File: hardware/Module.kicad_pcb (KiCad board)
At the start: 2 copper layers, 93.1 x 98.9 mm, 96 parts, among them J1 Power, J10 Jack, J11 A I/O, J12 Debug, J13 A IFACE, J2 B IFACE, J3 B I/O, J4 Jack, J5 Jack, J6 Jack, J7 Jack, J8 Jack, J9 Jack, SW2 Button, U1 MCP6004, U4 LM4040C10, U6 TL072, U9 MCP6002

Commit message: Prepare the schematic
Signed-off-by: Petr Horacek <hrck@protonmail.com>
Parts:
- moved A1 73.6 mm to (234.5, 48.2)
- moved RV4 53.4 mm to (229.4, 77.3)
- moved J5 49.9 mm to (237.4, 100.8)
- moved RV3 15.3 mm to (209.1, 95.6)

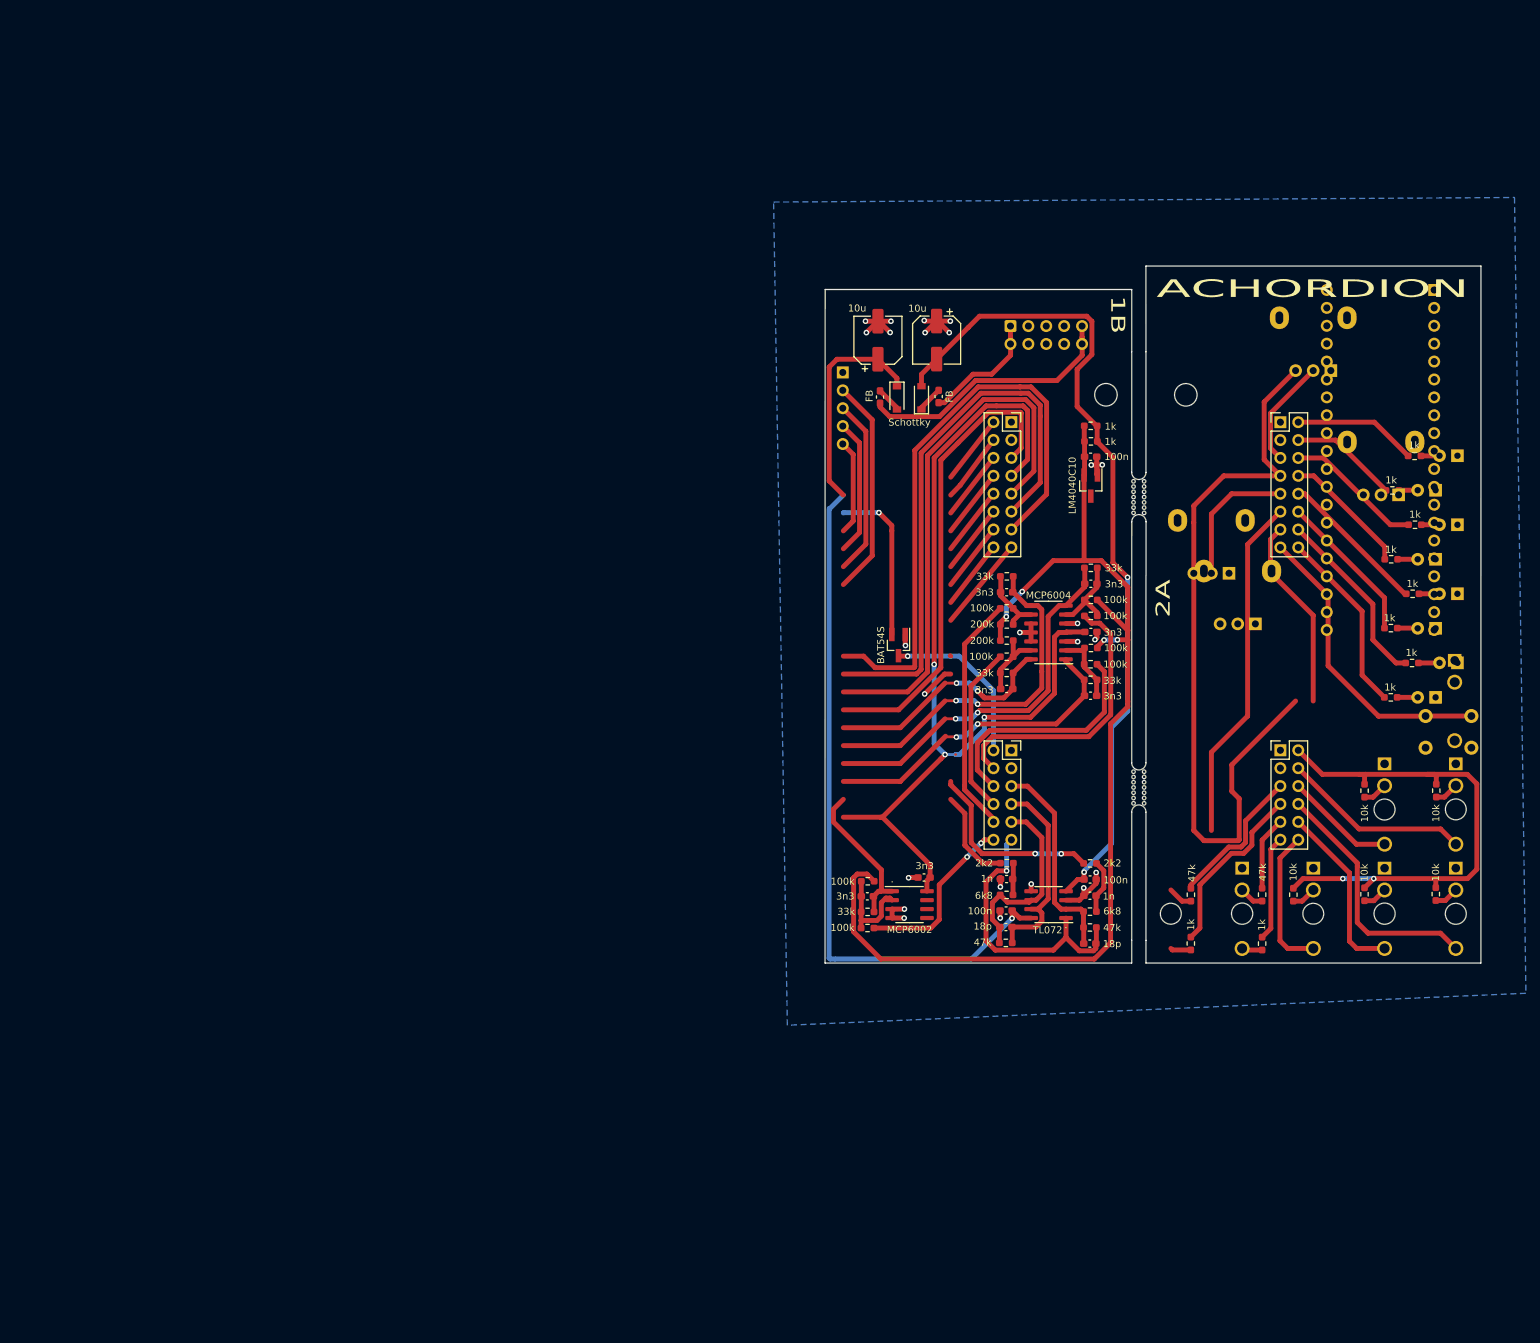
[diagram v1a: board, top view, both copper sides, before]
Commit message: Add SD card footprint
Signed-off-by: Petr Horacek <hrck@protonmail.com>
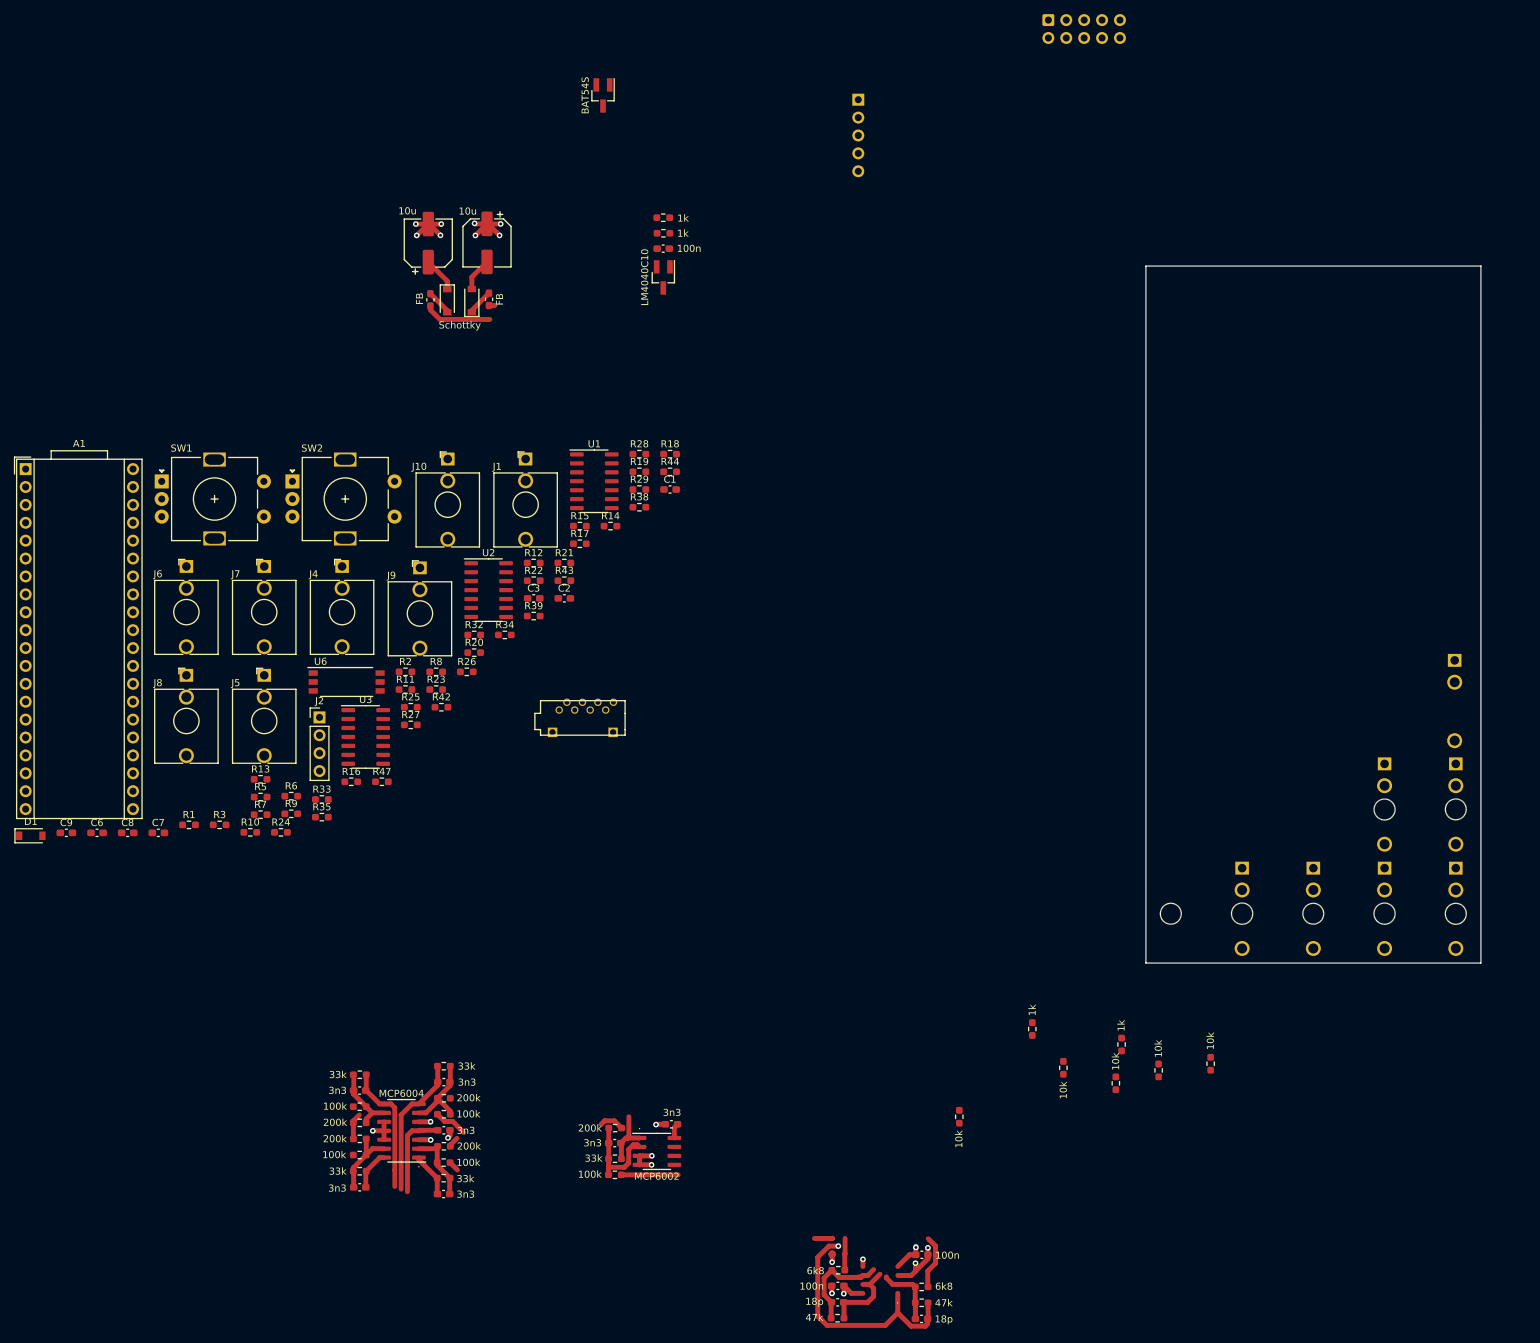
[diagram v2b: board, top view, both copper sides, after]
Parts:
- removed C35, C37: 1n, Capacitor_SMD:C_0603_1608Metric_Pad1.08x0.95mm_HandSolder
- removed D10, D5, D6, D7, D8, D9: LED, LED_THT:LED_D3.0mm
- removed the D3 at (234.7, 106.0)
- removed the D4 at (237.8, 101.2)
- removed the J11 at (212.6, 113.6)
- removed the J3 at (174.4, 113.6)
- removed the R36 at (231.3, 101.2)
- removed the R37 at (228.3, 96.2)
- removed the R40 at (231.7, 81.5)
- removed the R41 at (228.5, 76.7)
- removed the R50 at (199.9, 134.1)
- removed the R51 at (210.0, 134.1)
- removed REF** (x2): MountingHole_3.2mm_M3, MountingHole:MountingHole_3.2mm_M3
- removed RV1, RV2, RV3, RV4: B10k, Potentiometer_THT:Potentiometer_Alpha_RD901F-40-00D_Single_Vertical
- removed mouse-bite-2mm-slot (x2): VAL**, Panelization:mouse-bite-2mm-slot
- added C1: 100n, Capacitor_SMD:C_0603_1608Metric_Pad1.08x0.95mm_HandSolder, F.Cu at (126.0, 76.5)
- added C2: 18p, Capacitor_SMD:C_0603_1608Metric_Pad1.08x0.95mm_HandSolder, F.Cu at (111.0, 92.0)
- added C3: 18p, Capacitor_SMD:C_0603_1608Metric_Pad1.08x0.95mm_HandSolder, F.Cu at (106.7, 92.0)
- added C6: 100n, Capacitor_SMD:C_0603_1608Metric_Pad1.08x0.95mm_HandSolder, F.Cu at (44.7, 125.3)
- added C7: 100n, Capacitor_SMD:C_0603_1608Metric_Pad1.08x0.95mm_HandSolder, F.Cu at (53.4, 125.3)
- added C8: 100n, Capacitor_SMD:C_0603_1608Metric_Pad1.08x0.95mm_HandSolder, F.Cu at (49.0, 125.3)
- added C9: 100n, Capacitor_SMD:C_0603_1608Metric_Pad1.08x0.95mm_HandSolder, F.Cu at (40.3, 125.3)
- added D1: Schottky, Diode_SMD:D_SOD-123, F.Cu at (35.3, 125.7)
- added J1: Jack, Connector_Audio:Jack_3.5mm_QingPu_WQP-PJ398SM_Vertical_CircularHoles, F.Cu at (105.5, 72.2)
- added J10: Jack, Connector_Audio:Jack_3.5mm_QingPu_WQP-PJ398SM_Vertical_CircularHoles, F.Cu at (94.5, 72.2)
- added J4: Jack, Connector_Audio:Jack_3.5mm_QingPu_WQP-PJ398SM_Vertical_CircularHoles, F.Cu at (79.5, 87.5)
- added J5: Jack, Connector_Audio:Jack_3.5mm_QingPu_WQP-PJ398SM_Vertical_CircularHoles, F.Cu at (68.4, 102.9)
- added J6: Jack, Connector_Audio:Jack_3.5mm_QingPu_WQP-PJ398SM_Vertical_CircularHoles, F.Cu at (57.4, 87.5)
- added J7: Jack, Connector_Audio:Jack_3.5mm_QingPu_WQP-PJ398SM_Vertical_CircularHoles, F.Cu at (68.4, 87.5)
- added J8: Jack, Connector_Audio:Jack_3.5mm_QingPu_WQP-PJ398SM_Vertical_CircularHoles, F.Cu at (57.4, 102.9)
- added J9: Jack, Connector_Audio:Jack_3.5mm_QingPu_WQP-PJ398SM_Vertical_CircularHoles, F.Cu at (90.5, 87.7)
- added R1: 33R, Resistor_SMD:R_0603_1608Metric_Pad0.98x0.95mm_HandSolder, F.Cu at (57.7, 124.2)
- added R10: 100k, Resistor_SMD:R_0603_1608Metric_Pad0.98x0.95mm_HandSolder, F.Cu at (66.4, 125.2)
- added R12: 6k8, Resistor_SMD:R_0603_1608Metric_Pad0.98x0.95mm_HandSolder, F.Cu at (106.7, 87.0)
- added R13: 6k8, Resistor_SMD:R_0603_1608Metric_Pad0.98x0.95mm_HandSolder, F.Cu at (67.9, 117.7)
- added R14: 100k, Resistor_SMD:R_0603_1608Metric_Pad0.98x0.95mm_HandSolder, F.Cu at (117.6, 81.7)
- added R15: 100k, Resistor_SMD:R_0603_1608Metric_Pad0.98x0.95mm_HandSolder, F.Cu at (113.2, 81.7)
- added R16: 200k, Resistor_SMD:R_0603_1608Metric_Pad0.98x0.95mm_HandSolder, F.Cu at (80.8, 118.0)
- added R17: 200k, Resistor_SMD:R_0603_1608Metric_Pad0.98x0.95mm_HandSolder, F.Cu at (113.2, 84.2)
- added R18: 1k, Resistor_SMD:R_0603_1608Metric_Pad0.98x0.95mm_HandSolder, F.Cu at (126.0, 71.5)
- added R19: 1k, Resistor_SMD:R_0603_1608Metric_Pad0.98x0.95mm_HandSolder, F.Cu at (121.7, 74.0)
- added R2: 220R, Resistor_SMD:R_0603_1608Metric_Pad0.98x0.95mm_HandSolder, F.Cu at (88.5, 102.4)
- added R20: 100k, Resistor_SMD:R_0603_1608Metric_Pad0.98x0.95mm_HandSolder, F.Cu at (98.2, 99.7)
- added R21: 100k, Resistor_SMD:R_0603_1608Metric_Pad0.98x0.95mm_HandSolder, F.Cu at (111.0, 87.0)
- added R22: 33k, Resistor_SMD:R_0603_1608Metric_Pad0.98x0.95mm_HandSolder, F.Cu at (106.7, 89.5)
- added R23: 33k, Resistor_SMD:R_0603_1608Metric_Pad0.98x0.95mm_HandSolder, F.Cu at (92.8, 104.9)
- added R24: 33k, Resistor_SMD:R_0603_1608Metric_Pad0.98x0.95mm_HandSolder, F.Cu at (70.8, 125.2)
- added R25: 33k, Resistor_SMD:R_0603_1608Metric_Pad0.98x0.95mm_HandSolder, F.Cu at (89.2, 107.5)
- added R26: 100k, Resistor_SMD:R_0603_1608Metric_Pad0.98x0.95mm_HandSolder, F.Cu at (97.2, 102.4)
- added R27: 100k, Resistor_SMD:R_0603_1608Metric_Pad0.98x0.95mm_HandSolder, F.Cu at (89.2, 110.0)
- added R28: 100k, Resistor_SMD:R_0603_1608Metric_Pad0.98x0.95mm_HandSolder, F.Cu at (121.7, 71.5)
- added R29: 100k, Resistor_SMD:R_0603_1608Metric_Pad0.98x0.95mm_HandSolder, F.Cu at (121.7, 76.5)
- added R3: 10R, Resistor_SMD:R_0603_1608Metric_Pad0.98x0.95mm_HandSolder, F.Cu at (62.1, 124.2)
- added R32: 100R, Resistor_SMD:R_0603_1608Metric_Pad0.98x0.95mm_HandSolder, F.Cu at (98.2, 97.2)
- added R33: 100R, Resistor_SMD:R_0603_1608Metric_Pad0.98x0.95mm_HandSolder, F.Cu at (76.6, 120.5)
- added R34: 1k, Resistor_SMD:R_0603_1608Metric_Pad0.98x0.95mm_HandSolder, F.Cu at (102.6, 97.2)
- added R43: 47k, Resistor_SMD:R_0603_1608Metric_Pad0.98x0.95mm_HandSolder, F.Cu at (111.0, 89.5)
- added R44: 47k, Resistor_SMD:R_0603_1608Metric_Pad0.98x0.95mm_HandSolder, F.Cu at (126.0, 74.0)
- added R47: 10k, Resistor_SMD:R_0603_1608Metric_Pad0.98x0.95mm_HandSolder, F.Cu at (85.1, 118.0)
- added R5: 10k, Resistor_SMD:R_0603_1608Metric_Pad0.98x0.95mm_HandSolder, F.Cu at (67.9, 120.2)
- added R6: 47k, Resistor_SMD:R_0603_1608Metric_Pad0.98x0.95mm_HandSolder, F.Cu at (72.2, 120.1)
- added R8: 33k, Resistor_SMD:R_0603_1608Metric_Pad0.98x0.95mm_HandSolder, F.Cu at (92.8, 102.4)
- added R9: 33k, Resistor_SMD:R_0603_1608Metric_Pad0.98x0.95mm_HandSolder, F.Cu at (72.2, 122.6)
- added SW1: Encoder, Rotary_Encoder:RotaryEncoder_Alps_EC11E-Switch_Vertical_H20mm, F.Cu at (53.9, 75.4)
- added U2: TL074, Package_SO:SOIC-14_3.9x8.7mm_P1.27mm, F.Cu at (100.3, 90.8)
- added U3: TL074, Package_SO:SOIC-14_3.9x8.7mm_P1.27mm, F.Cu at (82.8, 111.7)
- added U4: MCP6004, Package_SO:SOIC-14_3.9x8.7mm_P1.27mm, F.Cu at (87.9, 167.6)
- A1: moved to F.Cu
- J13: value A IFACE -> Micro_SD; footprint Connector_PinHeader_2.54mm:PinHeader_2x08_P2.54mm_Vertical -> Custom:microsd_connector
- J2: value B IFACE -> OLED; footprint Connector_PinSocket_2.54mm:PinSocket_2x08_P2.54mm_Vertical -> Connector_PinHeader_2.54mm:PinHeader_1x04_P2.54mm_Vertical
- R11: value 2k2 -> 100k
- R38, R39, R42: value 1k -> 47k
- R48: renamed from R20; value 100k -> 200k
- R52: renamed from R23; value 100k -> 200k
- R59: renamed from R17; value 100k -> 200k
- R7: value 2k2 -> 47k
- SW2: value Button -> Encoder; footprint Button_Switch_THT:SW_PUSH_6mm -> Rotary_Encoder:RotaryEncoder_Alps_EC11E-Switch_Vertical_H20mm; moved to F.Cu
- U1: value MCP6004 -> TL074
- U6: value TL072 -> TLP2361; footprint Package_SO:SOIC-8_3.9x4.9mm_P1.27mm -> Package_SO:SO-6L_10x3.84mm_P1.27mm
- moved A1 201.5 mm to (34.5, 73.7), turned to 0 degrees
- moved SW2 170.6 mm to (72.4, 75.4), turned to 0 degrees
- moved R35 152.7 mm to (76.6, 123.0)
- moved R42 142.7 mm to (93.6, 107.5)
- moved R39 122.0 mm to (106.7, 94.5)
- moved R7 117.9 mm to (67.9, 122.7)
- moved R65 115.9 mm to (82.0, 159.6)
- moved C17 115.9 mm to (93.9, 176.6)
- moved C18 115.9 mm to (82.0, 161.9)
- moved R50 115.9 mm to (82.0, 168.7)
- moved R59 115.9 mm to (93.9, 169.8)
- moved R61 115.9 mm to (82.0, 166.4)
- moved C13 115.9 mm to (82.0, 175.6)
- moved C15 115.9 mm to (93.9, 167.5)
- moved R49 115.9 mm to (93.9, 165.2)
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- renumbered C33 to C10, C34 to C11, C41 to C12, C43 to C13, C44 to C14, C46 to C15, C48 to C16, C40 to C17, C42 to C18, C38 to C4, C36 to C5, D11 to D2, D1 to D3, D2 to D4, J5 to J11, J4 to J12, J6 to J14, J8 to J15, J10 to J16, J1 to J17, J7 to J18, J9 to J19, J12 to J3, R12 to R30, R8 to R31, R13 to R36, R9 to R37, R48 to R4, R14 to R40, R10 to R41, R43 to R45, R21 to R49, R27 to R50, R28 to R51, R30 to R53, R22 to R54, R29 to R55, R31 to R56, R45 to R57, R47 to R58, R18 to R60, R24 to R61, R25 to R62, R4 to R63, R19 to R64, R26 to R65, R5 to R66, U9 to U5, U4 to U7
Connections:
- A1 pad 1: B_LED8 -> Net-(A1-Pad1)
- A1 pad 11: B_PROBE -> Net-(A1-Pad11)
- A1 pad 12: VERSION_A -> OLED_SCL
- A1 pad 13: VERSION_A -> OLED_SDA
- A1 pad 14: VERSION_A -> Net-(A1-Pad14)
- A1 pad 15: VERSION_A -> Net-(A1-Pad15)
- A1 pad 16: Net-(A1-Pad16) -> AUDIO_IN1
- A1 pad 17: Net-(A1-Pad17) -> AUDIO_IN2
- A1 pad 18: DAC1 -> AUDIO_OUT1
- A1 pad 19: DAC2 -> AUDIO_OUT2
- A1 pad 2: B_LED7 -> SD_D3
- A1 pad 20: VERSION_A -> GND
- A1 pad 27: B_POT1 -> MIDI_OUT
- A1 pad 28: B_POT2 -> MIDI_IN
- A1 pad 29: B_POT4 -> DAC1
- A1 pad 3: B_LED6 -> SD_D2
- A1 pad 30: B_POT3 -> DAC2
- A1 pad 31: Net-(A1-Pad31) -> ENC1_A
- A1 pad 32: Net-(A1-Pad32) -> ENC1_B
- A1 pad 33: Net-(A1-Pad33) -> ENC2_A
- A1 pad 34: GPIO1 -> ENC2_B
- A1 pad 35: GPIO2 -> Net-(A1-Pad35)
- A1 pad 36: GPIO3 -> Net-(A1-Pad36)
- A1 pad 37: GPIO4 -> Net-(A1-Pad37)
- A1 pad 4: B_LED5 -> SD_D1
- A1 pad 40: VERSION_A -> GND
- A1 pad 5: B_LED4 -> SD_D0
- A1 pad 6: B_LED3 -> SD_CMD
- A1 pad 7: B_LED2 -> SD_CK
- A1 pad 8: B_LED1 -> ENC1_CLICK
- A1 pad 9: B_BUTTON -> ENC2_CLICK
- C10 pad 2: VERSION_A -> GND
- C11 pad 1: VERSION_A -> GND
- C12 pad 2: Net-(C41-Pad2) -> Net-(C12-Pad2)
- C13 pad 2: Net-(C43-Pad2) -> Net-(C13-Pad2)
- C15 pad 1: VERSION_A -> GND
- C16 pad 1: VERSION_A -> GND
- C17 pad 2: Net-(C40-Pad2) -> Net-(C17-Pad2)
- C18 pad 2: Net-(C42-Pad2) -> Net-(C18-Pad2)
- C19 pad 2: VERSION_A -> GND
- C20 pad 1: VERSION_A -> GND
- C21 pad 2: VERSION_A -> GND
- C4 pad 1: B_OUT2_MAIN -> Net-(C4-Pad1)
- C4 pad 2: B_OUT1_FALL -> Net-(C4-Pad2)
- C5 pad 1: B_OUT1_MAIN -> Net-(C5-Pad1)
- C5 pad 2: B_OUT2_FALL -> Net-(C5-Pad2)
- D2 pad 1: VERSION_A -> GND
- D2 pad 3: B_PROBE -> PROBE
- J11 pad S: VERSION_A -> GND
- J12 pad S: VERSION_A -> GND
- J14 pad S: VERSION_A -> GND
- J14 pad T: A_CV1_IN -> Net-(J14-PadT)
- J15 pad S: VERSION_A -> GND
- J15 pad T: A_CV3_IN -> Net-(J15-PadT)
- J16 pad S: VERSION_A -> GND
- J16 pad T: A_CV5_IN -> Net-(J16-PadT)
- J16 pad TN: Net-(J10-PadTN) -> Net-(J16-PadTN)
- J17 pad 3: VERSION_A -> GND
- J17 pad 4: VERSION_A -> GND
- J17 pad 5: VERSION_A -> GND
- J17 pad 6: VERSION_A -> GND
- J17 pad 7: VERSION_A -> GND
- J17 pad 8: VERSION_A -> GND
- J18 pad S: VERSION_A -> GND
- J18 pad T: A_CV2_IN -> Net-(J18-PadT)
- J19 pad S: VERSION_A -> GND
- J19 pad T: A_CV4_IN -> Net-(J19-PadT)
- J2 pad 1: VERSION_A -> +3V3
- J2 pad 2: B_LED8 -> GND
- J2 pad 3: VERSION_A -> OLED_SCL
- J2 pad 4: B_LED7 -> OLED_SDA
- J3 pad 1: VERSION_A -> GND
- R11 pad 1: DAC2 -> DAC1
- R11 pad 2: Net-(C37-Pad1) -> Net-(R11-Pad2)
- R30 pad 1: Net-(C37-Pad1) -> AUDIO_OUT2
- R30 pad 2: B_OUT1_FALL -> Net-(C4-Pad2)
- R31 pad 1: Net-(C35-Pad1) -> AUDIO_OUT1
- R31 pad 2: B_OUT2_FALL -> Net-(C5-Pad2)
- R35 pad 1: A_LED1 -> Net-(R29-Pad2)
- R36 pad 1: B_OUT1_FALL -> Net-(C4-Pad2)
- R36 pad 2: B_OUT2_MAIN -> Net-(C4-Pad1)
- R37 pad 1: B_OUT2_FALL -> Net-(C5-Pad2)
- R37 pad 2: B_OUT1_MAIN -> Net-(C5-Pad1)
- R38 pad 1: A_LED4 -> +3V3
- R38 pad 2: Net-(D6-Pad2) -> SD_D1
- R39 pad 1: A_LED5 -> +3V3
- R39 pad 2: Net-(D7-Pad2) -> SD_D0
- R4 pad 1: A_PROBE -> PROBE
- R4 pad 2: Net-(J10-PadTN) -> Net-(J5-PadTN)
- R40 pad 1: A_OUT2_MAIN -> Net-(C4-Pad1)
- R41 pad 1: A_OUT1_MAIN -> Net-(C5-Pad1)
- R42 pad 1: A_LED8 -> +3V3
- R42 pad 2: Net-(D10-Pad2) -> SD_CMD
- R45 pad 1: A_PROBE -> PROBE
- R46 pad 1: A_PROBE -> PROBE
- R48 pad 2: Net-(C41-Pad2) -> Net-(C12-Pad2)
- R49 pad 1: B_CV1_IN -> Net-(J14-PadT)
- R49 pad 2: Net-(C41-Pad2) -> Net-(C12-Pad2)
- R50 pad 2: Net-(C43-Pad2) -> Net-(C13-Pad2)
- R51 pad 1: B_CV3_IN -> Net-(J15-PadT)
- R51 pad 2: Net-(C43-Pad2) -> Net-(C13-Pad2)
- R53 pad 1: B_CV5_IN -> Net-(J16-PadT)
- R54 pad 1: Net-(C41-Pad2) -> Net-(C12-Pad2)
- R55 pad 1: Net-(C43-Pad2) -> Net-(C13-Pad2)
- R57 pad 1: A_PROBE -> PROBE
- R58 pad 1: A_PROBE -> PROBE
- R59 pad 2: Net-(C40-Pad2) -> Net-(C17-Pad2)
- R60 pad 1: B_CV2_IN -> Net-(J18-PadT)
- R60 pad 2: Net-(C40-Pad2) -> Net-(C17-Pad2)
- R61 pad 2: Net-(C42-Pad2) -> Net-(C18-Pad2)
- R62 pad 1: B_CV4_IN -> Net-(J19-PadT)
- R62 pad 2: Net-(C42-Pad2) -> Net-(C18-Pad2)
- R64 pad 1: Net-(C40-Pad2) -> Net-(C17-Pad2)
- R65 pad 1: Net-(C42-Pad2) -> Net-(C18-Pad2)
- R7 pad 1: DAC1 -> Net-(J6-PadT)
- R7 pad 2: Net-(C35-Pad1) -> Net-(C3-Pad2)
- U1 pad 1: CV2 -> Net-(R14-Pad2)
- U1 pad 10: VERSION_A -> GND
- U1 pad 11: VERSION_A -> VEE
- U1 pad 12: VERSION_A -> GND
- U1 pad 13: Net-(C43-Pad2) -> Net-(R21-Pad2)
- U1 pad 14: CV3 -> Net-(R27-Pad2)
- U1 pad 2: Net-(C40-Pad2) -> Net-(R14-Pad1)
- U1 pad 3: VERSION_A -> GND
- U1 pad 4: +3.3VA -> VCC
- U1 pad 5: VERSION_A -> GND
- U1 pad 6: Net-(C41-Pad2) -> Net-(R20-Pad2)
- U1 pad 7: CV1 -> Net-(R26-Pad2)
- U1 pad 8: CV4 -> Net-(R15-Pad2)
- U1 pad 9: Net-(C42-Pad2) -> Net-(R15-Pad1)
- U5 pad 3: VERSION_A -> GND
- U5 pad 4: VERSION_A -> GND
- U6 pad 1: B_OUT1_MAIN -> Net-(D1-Pad1)
- U6 pad 2: B_OUT2_FALL -> Net-(U6-Pad2)
- U6 pad 3: VERSION_A -> Net-(D1-Pad2)
- U6 pad 4: VEE -> GND
- U6 pad 5: VERSION_A -> MIDI_IN
- U6 pad 6: B_OUT1_FALL -> +3V3
- U7 pad 1: VERSION_A -> GND
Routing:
- net +3.3VA: track 242.8 -> 14.7 mm, vias 3 -> 0
- net -10V: track 158.6 -> 8.81 mm, vias 4 -> 0
- net VCC: track 130.5 -> 9.21 mm
- net VEE: track 118.8 -> 9.22 mm, vias 2 -> 1
- net B_POT3: track 85.0 -> 0.00 mm
- net B_POT4: track 80.0 -> 0.00 mm
- net B_POT2: track 76.2 -> 0.00 mm
- net A_PROBE: track 73.8 -> 0.00 mm, vias 2 -> 0
- net B_POT1: track 67.0 -> 0.00 mm
- net VERSION_A: track 53.5 -> 0.00 mm, vias 24 -> 0
- net A_POT4: track 49.3 -> 0.00 mm
- net A_BUTTON: track 42.9 -> 0.00 mm
- net GND: track 0.00 -> 42.9 mm, vias 0 -> 20
- net B_OUT1_MAIN: track 40.2 -> 0.00 mm, vias 1 -> 0
- net B_CV1_IN: track 39.9 -> 0.00 mm
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- removed copper zone on B.Cu, net VERSION_A
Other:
- board size 93.1 x 98.9 mm -> 47.6 x 98.9 mm
- board text removed: "1"
- board text removed: "1B"
- board text removed: "2"
- board text removed: "2A"
- board text removed: "2B"
- board text removed: "3"
- board text removed: "4"
- board text removed: "ACHORDION"
- board text removed: "GND"
- board text removed: "board v1.3.1"
- board text removed: "by ZLOSYNTH"

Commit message: Design the PCB
Signed-off-by: Petr Horacek <hrck@protonmail.com>
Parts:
- removed J3: Debug, Connector_PinHeader_2.54mm:PinHeader_1x05_P2.54mm_Vertical
- added G***: LOGO, Custom:outline, B.Cu at (136.5, 102.7)
- added REF**: MountingHole_2.2mm_M2, MountingHole:MountingHole_2.2mm_M2, F.Cu at (157.8, 74.9)
- J1, J4: footprint Connector_Audio:Jack_3.5mm_QingPu_WQP-PJ398SM_Vertical_CircularHoles -> Custom:Jack_3.5mm_QingPu_WQP-PJ398SM_Vertical_CircularHoles_Stereo; moved to B.Cu
- J10, J13, J5, J6, J7, J8, J9, SW1, SW2: moved to B.Cu
- J17: footprint Connector_IDC:IDC-Header_2x05_P2.54mm_Vertical -> Connector_PinHeader_2.54mm:PinHeader_2x05_P2.54mm_Vertical; moved to F.Cu
- J2: footprint Connector_PinHeader_2.54mm:PinHeader_1x04_P2.54mm_Vertical -> Connector_PinSocket_2.54mm:PinSocket_1x07_P2.54mm_Vertical; moved to B.Cu
- moved J11 128.6 mm to (116.3, 144.0)
- moved D1 119.1 mm to (153.5, 139.9), turned to 90 degrees
- moved D2 115.0 mm to (151.7, 130.1)
- moved J6 105.6 mm to (146.6, 144.0), turned to 180 degrees
- moved SW1 105.5 mm to (154.0, 108.7), turned to 90 degrees
- moved J17 104.8 mm to (117.8, 94.5), turned to 180 degrees
- moved C6 103.2 mm to (147.1, 137.5)
- moved A1 103.0 mm to (136.2, 57.3)
- moved J15 102.3 mm to (136.5, 114.1)
- moved J16 102.3 mm to (116.3, 114.1)
- moved J19 102.3 mm to (126.4, 114.1)
- moved R3 100.7 mm to (158.6, 152.9), turned to 270 degrees
- moved J2 96.9 mm to (153.5, 50.5), turned to 90 degrees
- moved J4 95.7 mm to (156.7, 144.0), turned to 180 degrees
- moved R1 95.4 mm to (149.7, 149.3), turned to 90 degrees
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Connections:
- A1 pad 10: Net-(A1-Pad10) -> OLED_CMD
- A1 pad 11: Net-(A1-Pad11) -> OLED_DATA
- A1 pad 12: OLED_SCL -> Net-(A1-Pad12)
- A1 pad 13: OLED_SDA -> ENC2_CLICK
- A1 pad 14: Net-(A1-Pad14) -> ENC2_B
- A1 pad 15: Net-(A1-Pad15) -> ENC2_A
- A1 pad 16: AUDIO_IN1 -> AUDIO_IN2
- A1 pad 17: AUDIO_IN2 -> AUDIO_IN1
- A1 pad 22: CV5 -> CV1
- A1 pad 23: CV2 -> CV5
- A1 pad 24: CV1 -> CV2
- A1 pad 25: CV4 -> CV3
- A1 pad 26: CV3 -> CV4
- A1 pad 27: MIDI_OUT -> ENC1_CLICK
- A1 pad 28: MIDI_IN -> ENC1_A
- A1 pad 31: ENC1_A -> ENC1_B
- A1 pad 32: ENC1_B -> MIDI_IN
- A1 pad 33: ENC2_A -> MIDI_OUT
- A1 pad 34: ENC2_B -> GATE1
- A1 pad 35: Net-(A1-Pad35) -> GATE2
- A1 pad 37: Net-(A1-Pad37) -> OLED_RST
- A1 pad 8: ENC1_CLICK -> OLED_CS
- A1 pad 9: ENC2_CLICK -> OLED_SCK
- C12 pad 1: CV1 -> CV5
- C14 pad 1: CV5 -> CV1
- C6 pad 2: Net-(C6-Pad2) -> GND
- C7 pad 1: Net-(C6-Pad2) -> GND
- J2 pad 1: +3V3 -> GND
- J2 pad 2: GND -> +3V3
- J2 pad 3: OLED_SCL -> OLED_CS
- J2 pad 4: OLED_SDA -> OLED_CMD
- R10 pad 1: DAC1 -> DAC2
- R45 pad 2: Net-(J14-PadTN) -> Net-(J16-PadTN)
- R47 pad 2: Net-(J16-PadTN) -> Net-(J14-PadTN)
- R49 pad 1: Net-(J14-PadT) -> Net-(J18-PadT)
- R51 pad 1: Net-(J15-PadT) -> Net-(J19-PadT)
- R53 pad 1: Net-(J16-PadT) -> Net-(J14-PadT)
- R54 pad 2: CV1 -> CV5
- R56 pad 2: CV5 -> CV1
- R60 pad 1: Net-(J18-PadT) -> Net-(J15-PadT)
- R62 pad 1: Net-(J19-PadT) -> Net-(J16-PadT)
- U4 pad 7: CV1 -> CV5
- U5 pad 1: CV5 -> CV1
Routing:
- net VCC: track 9.21 -> 267.2 mm, vias 1 -> 7
- net +3V3: track 0.00 -> 178.6 mm, vias 0 -> 3
- net VEE: track 9.22 -> 156.2 mm, vias 1 -> 4
- net PROBE: track 0.00 -> 102.1 mm, vias 0 -> 4
- net -10V: track 8.81 -> 104.5 mm, vias 0 -> 13
- net MIDI_IN: track 0.00 -> 94.9 mm, vias 0 -> 6
- net GND: track 42.9 -> 127.6 mm, vias 20 -> 37
- net MIDI_OUT: track 0.00 -> 81.4 mm, vias 0 -> 3
- net +3.3VA: track 14.7 -> 84.1 mm, vias 0 -> 9
- net DAC2: track 2.56 -> 69.1 mm, vias 0 -> 4
- net DAC1: track 0.00 -> 64.7 mm, vias 0 -> 4
- net GATE2: track 0.00 -> 63.1 mm, vias 0 -> 2
- net GATE1: track 0.00 -> 59.2 mm, vias 0 -> 2
- net AUDIO_IN2: track 0.00 -> 48.3 mm
- net CV3: track 5.64 -> 53.5 mm
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- added copper zone on B.Cu, net GND
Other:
- board size 47.6 x 98.9 mm -> 47.6 x 109.2 mm
- board text added: "-"
- board text added: "All headers go on this side of the PCB"
- board text added: "OLED"
- board text added: "Petr Horáček <petr@zlosynth.com>, 2022, CC BY-SA"
- board text added: "Proton,"
- board text added: "RED -12 V"
- board text added: "S. jack"
- board text added: "S/N:"
- board text added: "SD connector"
- board text added: "Take care not to damage SMD parts while soldering"
- board text added: "board v0.1.0"
- board text removed: "1A"

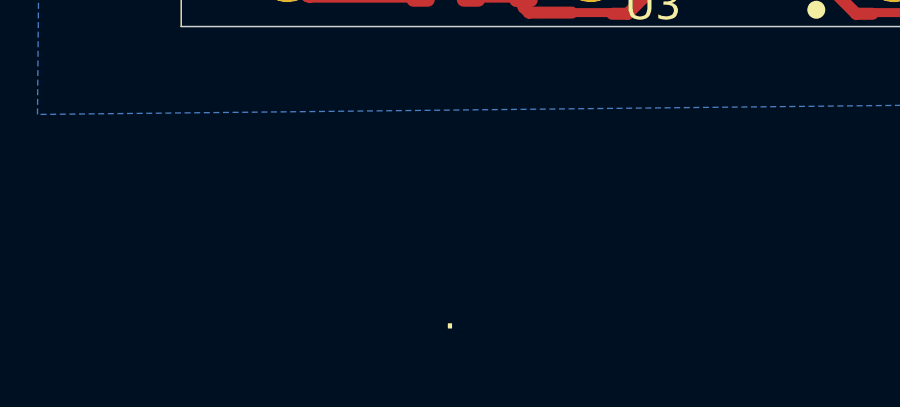
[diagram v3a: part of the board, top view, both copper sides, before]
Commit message: Remove a leftover dot on PCB
Signed-off-by: Petr Horacek <hrck@protonmail.com>
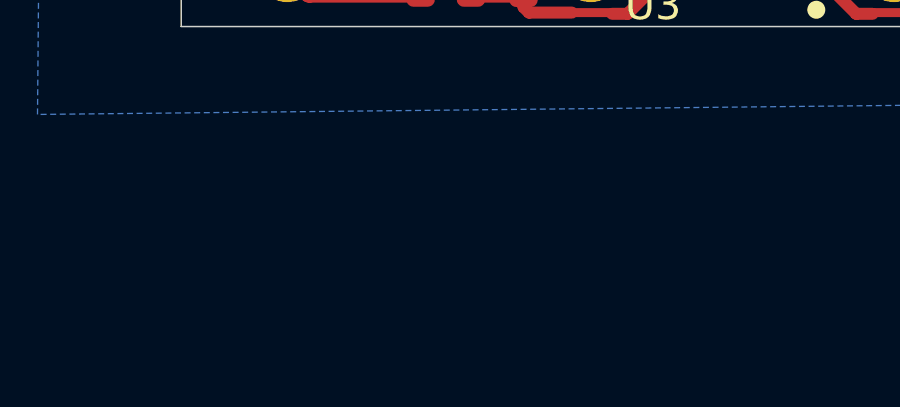
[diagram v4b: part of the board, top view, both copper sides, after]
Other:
- board text removed: "."
